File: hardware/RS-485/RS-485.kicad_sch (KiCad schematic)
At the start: 22 parts, among them J1 UART VSEL, J2 Screw_Terminal_01x06, J3 Half+, J4 Half-, J5 Conn_01x03_Pin, J6 Conn_01x16_Pin, J7 Conn_01x16_Pin, J8 Conn_01x01_Pin, P1 USB_C_Plug_USB2.0, U1 FT232HP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

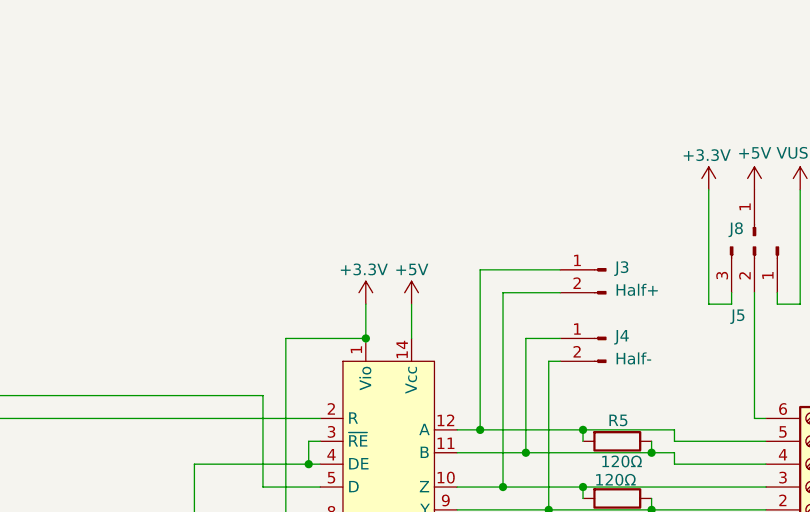
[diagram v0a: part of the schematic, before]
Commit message: Added README, gitignore.
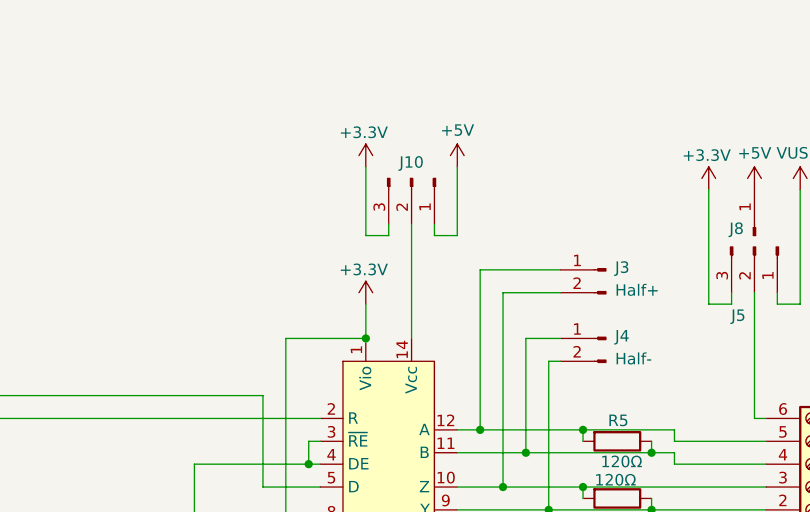
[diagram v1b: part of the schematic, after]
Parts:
- added J10: Conn_01x03_Pin, symbol Connector:Conn_01x03_Pin
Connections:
- net +3.3V: now also J10.3 (Pin_3)
- net +5V: now also J10.1 (Pin_1); no longer U2.14 (Vcc)
- new net: J10.2 (Pin_2), U2.14 (Vcc)
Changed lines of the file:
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@@
 	(wire
 		(pts
-			(xy 224.79 49.53) (xy 224.79 53.34)
+			(xy 224.79 40.64) (xy 224.79 53.34)
 		)
 		(stroke
@@
 	(wire
 		(pts
+			(xy 229.87 34.29) (xy 229.87 41.91)
+		)
+		(stroke
+			(width 0)
+			(type default)
+		)
+	)
+	(wire
+		(pts
 			(xy 116.84 118.11) (xy 116.84 120.65)
 		)
@@
 	(wire
 		(pts
+			(xy 219.71 41.91) (xy 219.71 34.29)
+		)
+		(stroke
+			(width 0)
+			(type default)
+		)
+	)
+	(wire
+		(pts
 			(xy 143.51 154.94) (xy 151.13 154.94)
 		)
@@
 	(wire
 		(pts
+			(xy 227.33 41.91) (xy 229.87 41.91)
+		)
+		(stroke
+			(width 0)
+			(type default)
+		)
+	)
+	(wire
+		(pts
 			(xy 109.22 105.41) (xy 125.73 105.41)
 		)
@@
 	(wire
 		(pts
+			(xy 222.25 40.64) (xy 222.25 41.91)
+		)
+		(stroke
+			(width 0)
+			(type default)
+		)
+	)
+	(wire
+		(pts
 			(xy 252.73 137.16) (xy 257.81 137.16)
 		)
@@
 	(wire
 		(pts
+			(xy 222.25 41.91) (xy 219.71 41.91)
+		)
+		(stroke
+			(width 0)
+			(type default)
+		)
+	)
+	(wire
+		(pts
 			(xy 262.89 74.93) (xy 262.89 78.74)
 		)
@@
 	(wire
 		(pts
+			(xy 227.33 40.64) (xy 227.33 41.91)
+		)
+		(stroke
+			(width 0)
+			(type default)
+		)
+	)
+	(wire
+		(pts
 			(xy 154.94 62.23) (xy 214.63 62.23)
 		)
@@
 	)
 	(symbol
-		(lib_id "power:+5V")
-		(at 224.79 49.53 0)
-		(unit 1)
-		(exclude_from_sim no)
-		(in_bom yes)
-		(on_board yes)
-		(dnp no)
-		(property "Reference" "#PWR04"
-			(at 224.79 53.34 0)
-			(effects
-				(font
-					(size 1.27 1.27)
-				)
-				(hide yes)
-			)
-		)
-		(property "Value" "+5V"
-			(at 224.79 45.72 0)
-			(effects
-				(font
-					(size 1.27 1.27)
-				)
-			)
-		)
-		(property "Footprint" ""
-			(at 224.79 49.53 0)
-			(effects
-				(font
-					(size 1.27 1.27)
-				)
-				(hide yes)
-			)
-		)
-		(property "Datasheet" ""
-			(at 224.79 49.53 0)
-			(effects
-				(font
-					(size 1.27 1.27)
-				)
-				(hide yes)
-			)
-		)
-		(property "Description" "Power symbol creates a global label with name \"+5V\""
-			(at 224.79 49.53 0)
-			(effects
-				(font
-					(size 1.27 1.27)
-				)
-				(hide yes)
-			)
-		)
-		(pin "1"
-		)
-		(instances
-			(project ""
-				(path "/943124bc-26a4-46d0-9560-d21a8397ce75"
-					(reference "#PWR04")
-					(unit 1)
-				)
-			)
-		)
-	)
-	(symbol
 		(lib_id "power:GND")
 		(at 116.84 120.65 0)
@@
 	)
 	(symbol
+		(lib_id "Connector:Conn_01x03_Pin")
+		(at 224.79 35.56 270)
+		(unit 1)
+		(exclude_from_sim no)
+		(in_bom yes)
+		(on_board yes)
+		(dnp no)
+		(property "Reference" "J10"
+			(at 224.79 33.782 90)
+			(effects
+				(font
+					(size 1.27 1.27)
+				)
+			)
+		)
+		(property "Value" "Conn_01x03_Pin"
+			(at 229.87 36.195 0)
+			(effects
+				(font
+					(size 1.27 1.27)
+				)
+				(hide yes)
+			)
+		)
+		(property "Footprint" ""
+			(at 224.79 35.56 0)
+			(effects
+				(font
+					(size 1.27 1.27)
+				)
+				(hide yes)
+			)
+		)
+		(property "Datasheet" "~"
+			(at 224.79 35.56 0)
+			(effects
+				(font
+					(size 1.27 1.27)
+				)
+				(hide yes)
+			)
+		)
+		(property "Description" "Generic connector, single row, 01x03, script generated"
+			(at 224.79 35.56 0)
+			(effects
+				(font
+					(size 1.27 1.27)
+				)
+				(hide yes)
+			)
+		)
+		(pin "3"
+		)
+		(pin "1"
+		)
+		(pin "2"
+		)
+		(instances
+			(project "RS-485"
+				(path "/943124bc-26a4-46d0-9560-d21a8397ce75"
+					(reference "J10")
+					(unit 1)
+				)
+			)
+		)
+	)
+	(symbol
 		(lib_id "power:+5V")
 		(at 116.84 140.97 0)
@@
 	)
 	(symbol
+		(lib_id "power:+5V")
+		(at 229.87 34.29 0)
+		(unit 1)
+		(exclude_from_sim no)
+		(in_bom yes)
+		(on_board yes)
+		(dnp no)
+		(property "Reference" "#PWR024"
+			(at 229.87 38.1 0)
+			(effects
+				(font
+					(size 1.27 1.27)
+				)
+				(hide yes)
+			)
+		)
+		(property "Value" "+5V"
+			(at 229.87 30.226 0)
+			(effects
+				(font
+					(size 1.27 1.27)
+				)
+			)
+		)
+		(property "Footprint" ""
+			(at 229.87 34.29 0)
+			(effects
+				(font
+					(size 1.27 1.27)
+				)
+				(hide yes)
+			)
+		)
+		(property "Datasheet" ""
+			(at 229.87 34.29 0)
+			(effects
+				(font
+					(size 1.27 1.27)
+				)
+				(hide yes)
+			)
+		)
+		(property "Description" "Power symbol creates a global label with name \"+5V\""
+			(at 229.87 34.29 0)
+			(effects
+				(font
+					(size 1.27 1.27)
+				)
+				(hide yes)
+			)
+		)
+		(pin "1"
+		)
+		(instances
+			(project "RS-485"
+				(path "/943124bc-26a4-46d0-9560-d21a8397ce75"
+					(reference "#PWR024")
+					(unit 1)
+				)
+			)
+		)
+	)
+	(symbol
 		(lib_id "power:GND")
 		(at 116.84 95.25 0)
@@
 					(unit 1)
 				)
+			)
+		)
+	)
+	(symbol
+		(lib_id "power:+3.3V")
+		(at 219.71 34.29 0)
+		(unit 1)
+		(exclude_from_sim no)
+		(in_bom yes)
+		(on_board yes)
+		(dnp no)
+		(property "Reference" "#PWR023"
+			(at 219.71 38.1 0)
+			(effects
+				(font
+					(size 1.27 1.27)
+				)
+				(hide yes)
+			)
+		)
+		(property "Value" "+3.3V"
+			(at 219.456 30.48 0)
+			(effects
+				(font
+					(size 1.27 1.27)
+				)
+			)
+		)
+		(property "Footprint" ""
+			(at 219.71 34.29 0)
+			(effects
+				(font
+					(size 1.27 1.27)
+				)
+				(hide yes)
+			)
+		)
+		(property "Datasheet" ""
+			(at 219.71 34.29 0)
+			(effects
+				(font
+					(size 1.27 1.27)
+				)
+				(hide yes)
+			)
+		)
+		(property "Description" "Power symbol creates a global label with name \"+3.3V\""
+			(at 219.71 34.29 0)
+			(effects
+				(font
+					(size 1.27 1.27)
+				)
+				(hide yes)
+			)
+		)
+		(pin "1"
+		)
+		(instances
+			(project "RS-485"
+				(path "/943124bc-26a4-46d0-9560-d21a8397ce75"
+					(reference "#PWR023")
+					(unit 1)
+				)

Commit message: Added info to title block.
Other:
- company: (none) -> Latency: Zero, LLC
- title: (none) -> USB-to-RS485 Adapter
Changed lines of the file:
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@@
 	(generator_version "8.0")
 	(paper "A4")
+	(title_block
+		(title "USB-to-RS485 Adapter")
+		(rev "1")
+		(company "Latency: Zero, LLC")
+		(comment 1 "©2024 Latency: Zero, LLC. All rights reserved.")
+	)
 	(junction
 		(at 67.31 139.7)

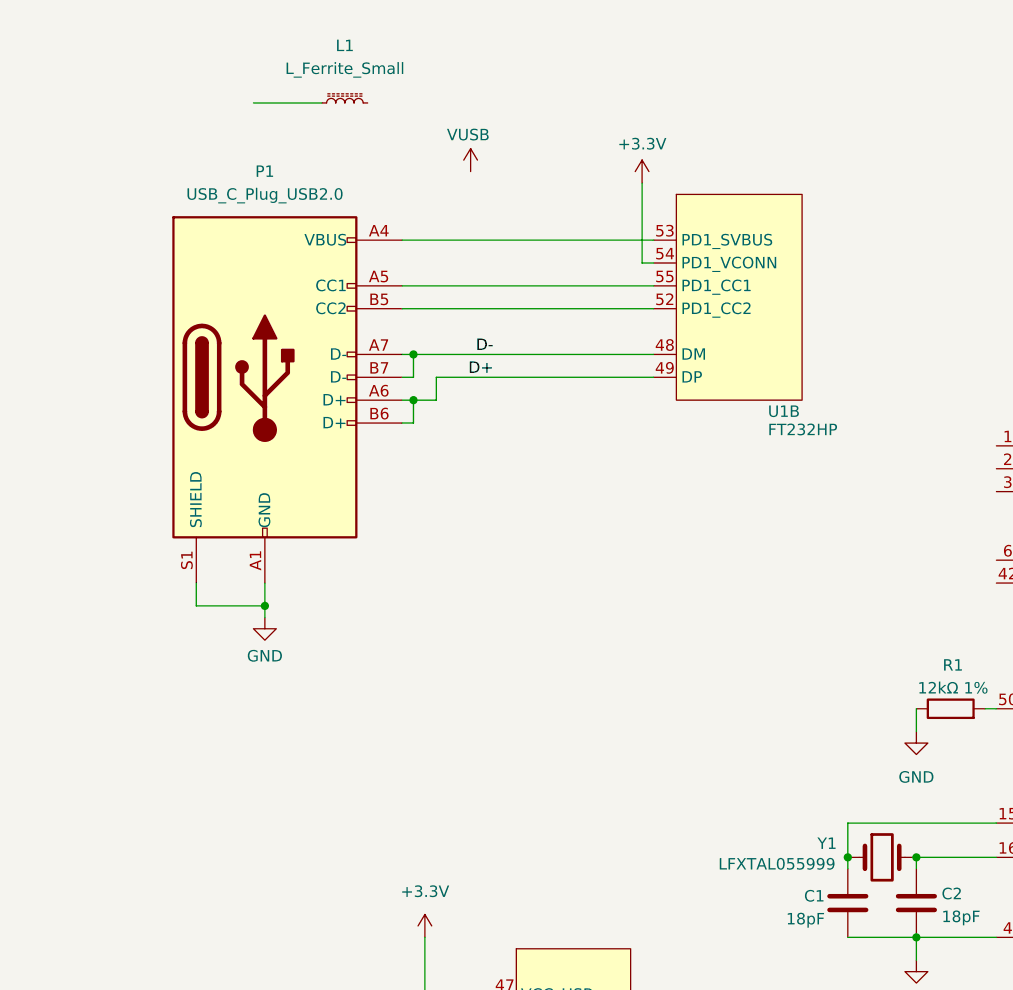
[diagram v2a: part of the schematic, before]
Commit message: Added TVS diodes to CC and D+/- lines
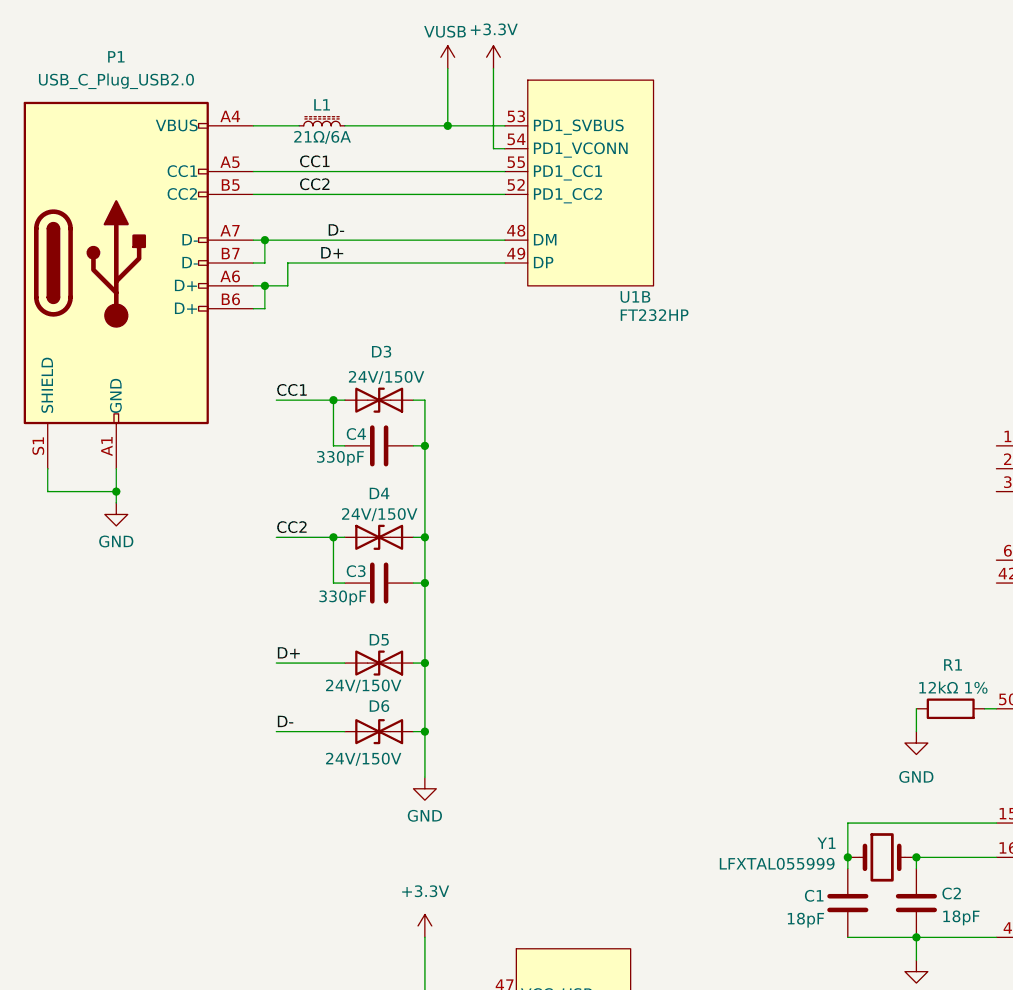
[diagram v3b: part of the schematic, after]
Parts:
- added C3, C4: 330pF, Capacitor_SMD:C_0603_1608Metric_Pad1.08x0.95mm_HandSolder, symbol Device:C
- added D3, D4, D5, D6: 24V/150V, symbol Device:D_TVS
- L1: value L_Ferrite_Small -> 21Ω/6A
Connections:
- net D+: now also D5.2 (A2)
- net D-: now also D6.2 (A2)
- net GND: now also C3.2, C4.2, D3.1 (A1), D4.2 (A2), D5.1 (A1), D6.1 (A1)
- net VUSB: now also L1.2, U1.53 (PD1_SVBUS)
- net CC2: now reaches P1.B5 (CC2), U1.52 (PD1_CC2)
- net CC2: now also C3.1, D4.1 (A1)
- net at P1.A4 (VBUS), P1.A9 (VBUS), P1.B4 (VBUS)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: now also L1.1; no longer U1.53 (PD1_SVBUS)
- net CC1: now reaches P1.A5 (CC1), U1.55 (PD1_CC1)
- net CC1: now also C4.1, D3.2 (A2)
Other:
- moved on the sheet: L1, P1, U1B
